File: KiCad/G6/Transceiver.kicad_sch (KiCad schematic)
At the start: 3 parts, among them U7 SN65HVD74DR

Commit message: sasha sneaky academic
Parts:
- added U1: ISL83488IBZ, CC0603KRXQRQBB104:SOIC8_4X5_INR, symbol ISL83488IBZ:ISL83488IBZ
- renumbered R5 to R4, R7 to R5, U7 to U9
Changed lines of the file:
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@@
 		(on_board yes)
 		(dnp no)
-		(property "Reference" "U7"
+		(property "Reference" "U9"
 			(at 124.46 86.36 0)
 			(effects
@@
 			(project "G6"
 				(path "/99017594-210d-4d15-87a7-3152ef0d7b7c/8222f4b1-36bd-45af-9e4f-a3e9ea2d7872"
-					(reference "U7")
+					(reference "U9")
+					(unit 1)
+				)
+			)
+		)
+	)
+	(symbol
+		(lib_id "ISL83488IBZ:ISL83488IBZ")
+		(at 194.31 95.25 0)
+		(unit 1)
+		(exclude_from_sim no)
+		(in_bom yes)
+		(on_board yes)
+		(dnp no)
+		(fields_autoplaced yes)
+		(property "Reference" "U1"
+			(at 214.63 85.09 0)
+			(effects
+				(font
+					(size 1.524 1.524)
+				)
+			)
+		)
+		(property "Value" "ISL83488IBZ"
+			(at 214.63 87.63 0)
+			(effects
+				(font
+					(size 1.524 1.524)
+				)
+			)
+		)
+		(property "Footprint" "CC0603KRXQRQBB104:SOIC8_4X5_INR"
+			(at 194.31 95.25 0)
+			(effects
+				(font
+					(size 1.27 1.27)
+					(italic yes)
+				)
+				(hide yes)
+			)
+		)
+		(property "Datasheet" "ISL83488IBZ"
+			(at 194.31 95.25 0)
+			(effects
+				(font
+					(size 1.27 1.27)
+					(italic yes)
+				)
+				(hide yes)
+			)
+		)
+		(property "Description" ""
+			(at 194.31 95.25 0)
+			(effects
+				(font
+					(size 1.27 1.27)
+				)
+				(hide yes)
+			)
+		)
+		(pin "4"
+		)
+		(pin "6"
+		)
+		(pin "5"
+		)
+		(pin "8"
+		)
+		(pin "1"
+		)
+		(pin "7"
+		)
+		(pin "2"
+		)
+		(pin "3"
+		)
+		(instances
+			(project "G6"
+				(path "/99017594-210d-4d15-87a7-3152ef0d7b7c/8222f4b1-36bd-45af-9e4f-a3e9ea2d7872"
+					(reference "U1")
 					(unit 1)
 				)
@@
 		(dnp no)
 		(fields_autoplaced yes)
-		(property "Reference" "R5"
+		(property "Reference" "R4"
 			(at 158.75 86.3599 90)
 			(effects
@@
 			(project "G6"
 				(path "/99017594-210d-4d15-87a7-3152ef0d7b7c/8222f4b1-36bd-45af-9e4f-a3e9ea2d7872"
-					(reference "R5")
+					(reference "R4")
 					(unit 1)
 				)
@@
 		(on_board yes)
 		(dnp no)
-		(property "Reference" "#PWR027"
+		(property "Reference" "#PWR040"
 			(at 95.25 104.14 0)
 			(effects
@@
 			(project "G6"
 				(path "/99017594-210d-4d15-87a7-3152ef0d7b7c/8222f4b1-36bd-45af-9e4f-a3e9ea2d7872"
-					(reference "#PWR027")
+					(reference "#PWR040")
 					(unit 1)
 				)
@@
 		(dnp no)
 		(fields_autoplaced yes)
-		(property "Reference" "R7"
+		(property "Reference" "R5"
 			(at 158.75 110.4899 90)
 			(effects
@@
 			(project "G6"
 				(path "/99017594-210d-4d15-87a7-3152ef0d7b7c/8222f4b1-36bd-45af-9e4f-a3e9ea2d7872"
-					(reference "R7")
-					(unit 1)
-				)
+					(reference "R5")
+					(unit 1)
+				)

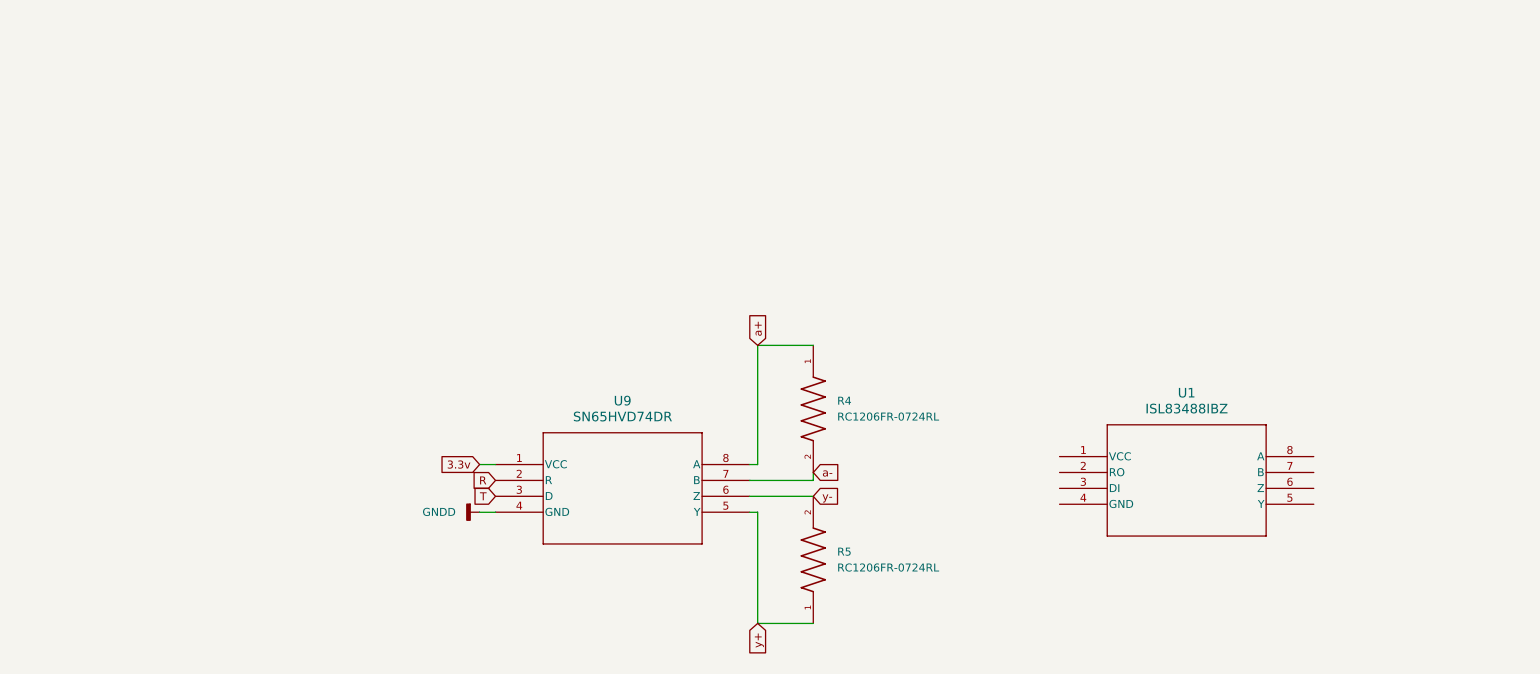
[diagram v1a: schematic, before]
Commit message: errrrrr i cant find a umcx connector they all say there like $50??
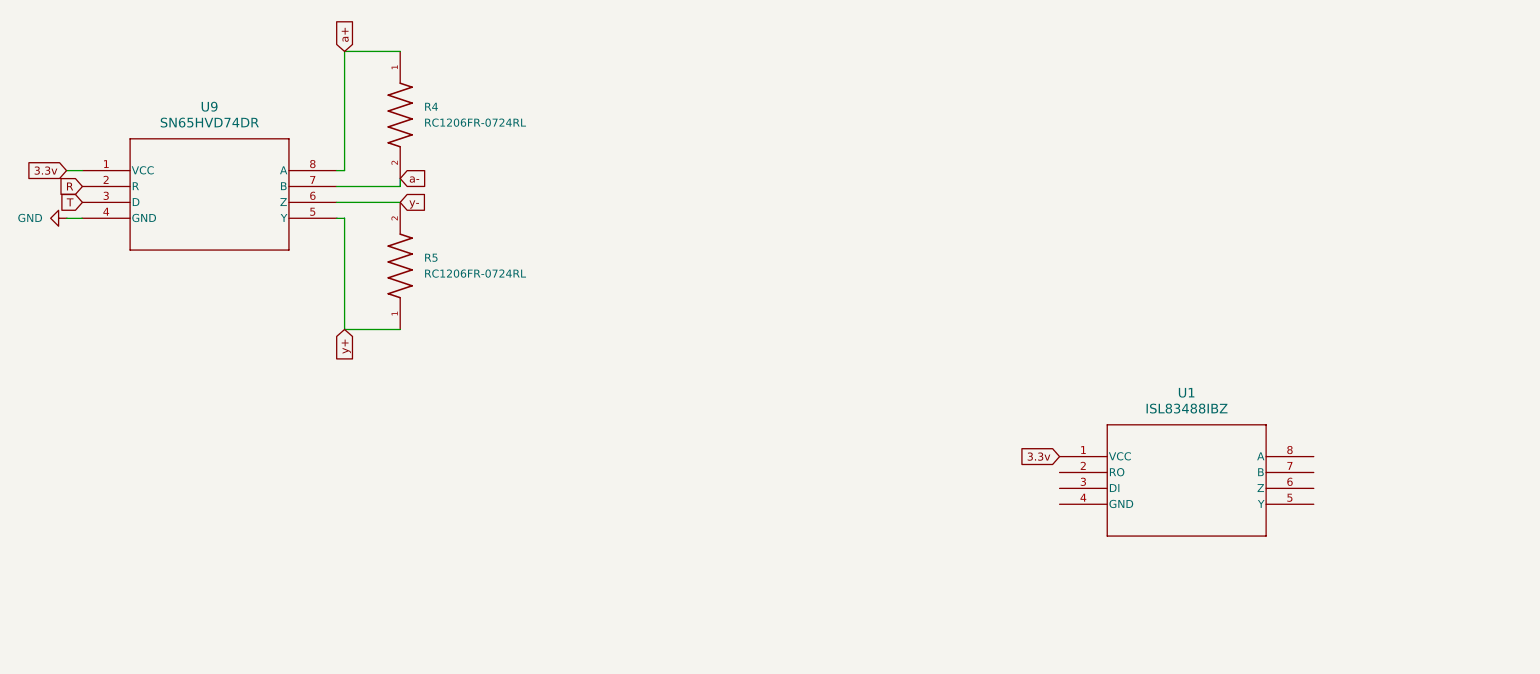
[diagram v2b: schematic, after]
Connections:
- net 3.3v: now also U1.1 (VCC)
- net GNDD renamed GND
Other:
- moved on the sheet: R4, R5, U9

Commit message: i have no idea whats going on, everything crashed and nothing will open
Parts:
- removed R4, R5: RC1206FR-0724RL, Resistor_SMD:R_1206_3216Metric, symbol RC1206FR-0724RL:RC1206FR-0724RL
- removed U9: SN65HVD74DR, 2N65HVD74DR:D8_TEX, symbol SN65HVD74DR Transceiver:SN65HVD74DR
- added R8, R9: RC1206FR-0724RL, Resistor_SMD:R_1206_3216Metric, symbol RC1206FR-0724RL:RC1206FR-0724RL
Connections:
- net GND: now also U1.4 (GND)
- net a+: now also U1.8 (A), R8.1
- net a-: now also U1.7 (B), R8.2
- net y+: now also U1.5 (Y), R9.1
- net y-: now also U1.6 (Z), R9.2
- net RX: now reaches U1.2 (RO)
- net TX: now reaches U1.3 (DI)

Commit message: g6
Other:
- moved on the sheet: R8, R9, U1
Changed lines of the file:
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@@
 	(wire
 		(pts
-			(xy 236.22 102.87) (xy 236.22 120.65)
-		)
-		(stroke
-			(width 0)
-			(type default)
-		)
-	)
-	(wire
-		(pts
-			(xy 245.11 100.33) (xy 234.95 100.33)
-		)
-		(stroke
-			(width 0)
-			(type default)
-		)
-	)
-	(wire
-		(pts
-			(xy 245.11 97.79) (xy 234.95 97.79)
-		)
-		(stroke
-			(width 0)
-			(type default)
-		)
-	)
-	(wire
-		(pts
-			(xy 236.22 76.2) (xy 245.11 76.2)
-		)
-		(stroke
-			(width 0)
-			(type default)
-		)
-	)
-	(wire
-		(pts
-			(xy 236.22 120.65) (xy 245.11 120.65)
-		)
-		(stroke
-			(width 0)
-			(type default)
-		)
-	)
-	(wire
-		(pts
-			(xy 245.11 96.52) (xy 245.11 97.79)
-		)
-		(stroke
-			(width 0)
-			(type default)
-		)
-	)
-	(wire
-		(pts
-			(xy 236.22 102.87) (xy 234.95 102.87)
-		)
-		(stroke
-			(width 0)
-			(type default)
-		)
-	)
-	(wire
-		(pts
-			(xy 236.22 76.2) (xy 236.22 95.25)
-		)
-		(stroke
-			(width 0)
-			(type default)
-		)
-	)
-	(wire
-		(pts
-			(xy 236.22 95.25) (xy 234.95 95.25)
+			(xy 151.13 96.52) (xy 151.13 114.3)
+		)
+		(stroke
+			(width 0)
+			(type default)
+		)
+	)
+	(wire
+		(pts
+			(xy 160.02 93.98) (xy 149.86 93.98)
+		)
+		(stroke
+			(width 0)
+			(type default)
+		)
+	)
+	(wire
+		(pts
+			(xy 160.02 91.44) (xy 149.86 91.44)
+		)
+		(stroke
+			(width 0)
+			(type default)
+		)
+	)
+	(wire
+		(pts
+			(xy 151.13 69.85) (xy 160.02 69.85)
+		)
+		(stroke
+			(width 0)
+			(type default)
+		)
+	)
+	(wire
+		(pts
+			(xy 151.13 114.3) (xy 160.02 114.3)
+		)
+		(stroke
+			(width 0)
+			(type default)
+		)
+	)
+	(wire
+		(pts
+			(xy 160.02 90.17) (xy 160.02 91.44)
+		)
+		(stroke
+			(width 0)
+			(type default)
+		)
+	)
+	(wire
+		(pts
+			(xy 151.13 96.52) (xy 149.86 96.52)
+		)
+		(stroke
+			(width 0)
+			(type default)
+		)
+	)
+	(wire
+		(pts
+			(xy 151.13 69.85) (xy 151.13 88.9)
+		)
+		(stroke
+			(width 0)
+			(type default)
+		)
+	)
+	(wire
+		(pts
+			(xy 151.13 88.9) (xy 149.86 88.9)
 		)
 		(stroke
@@
 	(global_label "a-"
 		(shape input)
-		(at 245.11 96.52 0)
+		(at 160.02 90.17 0)
 		(fields_autoplaced yes)
 		(effects
@@
 		)
 		(property "Intersheetrefs" "${INTERSHEET_REFS}"
-			(at 250.8166 96.52 0)
+			(at 165.7266 90.17 0)
 			(effects
 				(font
@@
 	(global_label "3.3v"
 		(shape input)
-		(at 194.31 95.25 180)
+		(at 109.22 88.9 180)
 		(fields_autoplaced yes)
 		(effects
@@
 		)
 		(property "Intersheetrefs" "${INTERSHEET_REFS}"
-			(at 187.3334 95.25 0)
+			(at 102.2434 88.9 0)
 			(effects
 				(font
@@
 	(global_label "a+"
 		(shape input)
-		(at 236.22 76.2 90)
+		(at 151.13 69.85 90)
 		(fields_autoplaced yes)
 		(effects
@@
 		)
 		(property "Intersheetrefs" "${INTERSHEET_REFS}"
-			(at 236.22 70.4934 90)
+			(at 151.13 64.1434 90)
 			(effects
 				(font
@@
 	(global_label "y-"
 		(shape input)
-		(at 245.11 100.33 0)
+		(at 160.02 93.98 0)
 		(fields_autoplaced yes)
 		(effects
@@
 		)
 		(property "Intersheetrefs" "${INTERSHEET_REFS}"
-			(at 250.6352 100.33 0)
+			(at 165.5452 93.98 0)
 			(effects
 				(font
@@
 	(global_label "y+"
 		(shape input)
-		(at 236.22 120.65 270)
+		(at 151.13 114.3 270)
 		(fields_autoplaced yes)
 		(effects
@@
 		)
 		(property "Intersheetrefs" "${INTERSHEET_REFS}"
-			(at 236.22 126.1752 90)
+			(at 151.13 119.8252 90)
 			(effects
 				(font
@@
 	(hierarchical_label "TX"
 		(shape input)
-		(at 194.31 100.33 180)
+		(at 109.22 93.98 180)
 		(effects
 			(font
@@
 	(hierarchical_label "RX"
 		(shape input)
-		(at 194.31 97.79 180)
+		(at 109.22 91.44 180)
 		(effects
 			(font
@@
 	(symbol
 		(lib_id "RC1206FR-0724RL:RC1206FR-0724RL")
-		(at 245.11 86.36 270)
+		(at 160.02 80.01 270)
 		(unit 1)
 		(exclude_from_sim no)
@@
 		(fields_autoplaced yes)
 		(property "Reference" "R8"
-			(at 248.92 85.0899 90)
+			(at 163.83 78.7399 90)
 			(effects
 				(font
@@
 		)
 		(property "Value" "RC1206FR-0724RL"
-			(at 248.92 87.6299 90)
+			(at 163.83 81.2799 90)
 			(effects
 				(font
@@
 		)
 		(property "Footprint" "Resistor_SMD:R_1206_3216Metric"
-			(at 245.11 86.36 0)
+			(at 160.02 80.01 0)
 			(effects
 				(font
@@
 		)
 		(property "Datasheet" ""
-			(at 245.11 86.36 0)
+			(at 160.02 80.01 0)
 			(effects
 				(font
@@
 		)
 		(property "Description" ""
-			(at 245.11 86.36 0)
+			(at 160.02 80.01 0)
 			(effects
 				(font
@@
 	(symbol
 		(lib_id "RC1206FR-0724RL:RC1206FR-0724RL")
-		(at 245.11 110.49 90)
+		(at 160.02 104.14 90)
 		(unit 1)
 		(exclude_from_sim no)
@@
 		(fields_autoplaced yes)
 		(property "Reference" "R9"
-			(at 248.92 109.2199 90)
+			(at 163.83 102.8699 90)
 			(effects
 				(font
@@
 		)
 		(property "Value" "RC1206FR-0724RL"
-			(at 248.92 111.7599 90)
+			(at 163.83 105.4099 90)
 			(effects
 				(font
@@
 		)
 		(property "Footprint" "Resistor_SMD:R_1206_3216Metric"
-			(at 245.11 110.49 0)
+			(at 160.02 104.14 0)
 			(effects
 				(font
@@
 		)
 		(property "Datasheet" ""
-			(at 245.11 110.49 0)
+			(at 160.02 104.14 0)
 			(effects
 				(font
@@
 		)
 		(property "Description" ""
-			(at 245.11 110.49 0)
+			(at 160.02 104.14 0)
 			(effects
 				(font
@@
 	(symbol
 		(lib_id "ISL83488IBZ:ISL83488IBZ")
-		(at 194.31 95.25 0)
+		(at 109.22 88.9 0)
 		(unit 1)
 		(exclude_from_sim no)
@@
 		(fields_autoplaced yes)
 		(property "Reference" "U1"
-			(at 214.63 85.09 0)
+			(at 129.54 78.74 0)
 			(effects
 				(font
@@
 		)
 		(property "Value" "ISL83488IBZ"
-			(at 214.63 87.63 0)
+			(at 129.54 81.28 0)
 			(effects
 				(font
@@
 		)
 		(property "Footprint" "CC0603KRXQRQBB104:SOIC8_4X5_INR"
-			(at 194.31 95.25 0)
+			(at 109.22 88.9 0)
 			(effects
 				(font
@@
 		)
 		(property "Datasheet" "ISL83488IBZ"
-			(at 194.31 95.25 0)
+			(at 109.22 88.9 0)
 			(effects
 				(font
@@
 		)
 		(property "Description" ""
-			(at 194.31 95.25 0)
+			(at 109.22 88.9 0)
 			(effects
 				(font
@@
 	(symbol
 		(lib_id "power:GND")
-		(at 194.31 102.87 270)
+		(at 109.22 96.52 270)
 		(unit 1)
 		(exclude_from_sim no)
@@
 		(fields_autoplaced yes)
 		(property "Reference" "#PWR052"
-			(at 187.96 102.87 0)
+			(at 102.87 96.52 0)
 			(effects
 				(font
@@
 		)
 		(property "Value" "GND"
-			(at 190.5 102.8699 90)
+			(at 105.41 96.5199 90)
 			(effects
 				(font
@@
 		)
 		(property "Footprint" ""
-			(at 194.31 102.87 0)
+			(at 109.22 96.52 0)
 			(effects
 				(font
@@
 		)
 		(property "Datasheet" ""
-			(at 194.31 102.87 0)
+			(at 109.22 96.52 0)
 			(effects
 				(font
@@
 		)
 		(property "Description" "Power symbol creates a global label with name \"GND\" , ground"
-			(at 194.31 102.87 0)
-			(effects
-				(font
+			(at 109.22 96.52 0)
+			(effects
+				(font

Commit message: netclasses SUCK
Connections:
- net a+ renamed rx+
- net a- renamed rx-
- net y+ renamed tx+
- net y- renamed tx-
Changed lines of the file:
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@@
 		)
 	)
-	(global_label "a-"
+	(global_label "rx-"
 		(shape input)
 		(at 160.02 90.17 0)
@@
 		)
 		(property "Intersheetrefs" "${INTERSHEET_REFS}"
-			(at 165.7266 90.17 0)
+			(at 166.3919 90.17 0)
 			(effects
 				(font
@@
 		)
 	)
-	(global_label "a+"
+	(global_label "rx+"
 		(shape input)
 		(at 151.13 69.85 90)
@@
 		)
 		(property "Intersheetrefs" "${INTERSHEET_REFS}"
-			(at 151.13 64.1434 90)
+			(at 151.13 63.4781 90)
 			(effects
 				(font
@@
 		)
 	)
-	(global_label "y-"
+	(global_label "tx-"
 		(shape input)
 		(at 160.02 93.98 0)
@@
 		)
 		(property "Intersheetrefs" "${INTERSHEET_REFS}"
-			(at 165.5452 93.98 0)
+			(at 166.3314 93.98 0)
 			(effects
 				(font
@@
 		)
 	)
-	(global_label "y+"
+	(global_label "tx+"
 		(shape input)
 		(at 151.13 114.3 270)
@@
 		)
 		(property "Intersheetrefs" "${INTERSHEET_REFS}"
-			(at 151.13 119.8252 90)
+			(at 151.13 120.6114 90)
 			(effects
 				(font
